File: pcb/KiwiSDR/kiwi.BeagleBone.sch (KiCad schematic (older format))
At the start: 18 parts, among them U1 Artix-7 A35, U301 EEPROM 32Kx8

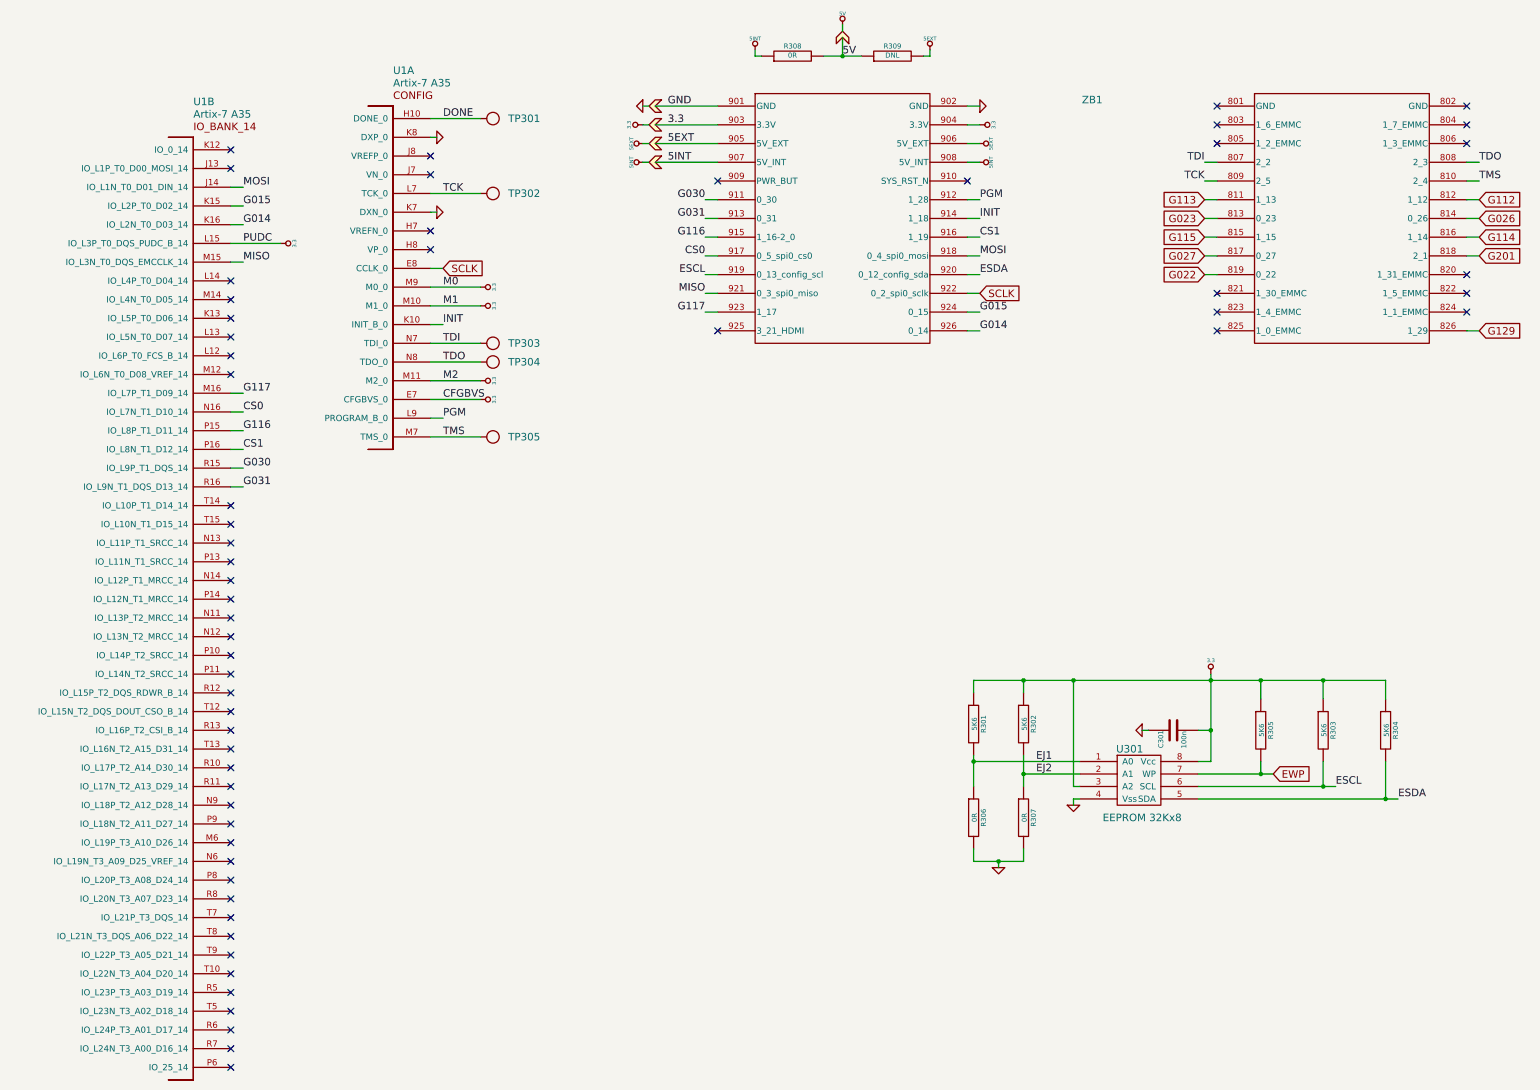
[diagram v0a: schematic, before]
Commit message: v0.5 PCB with 5V DC input
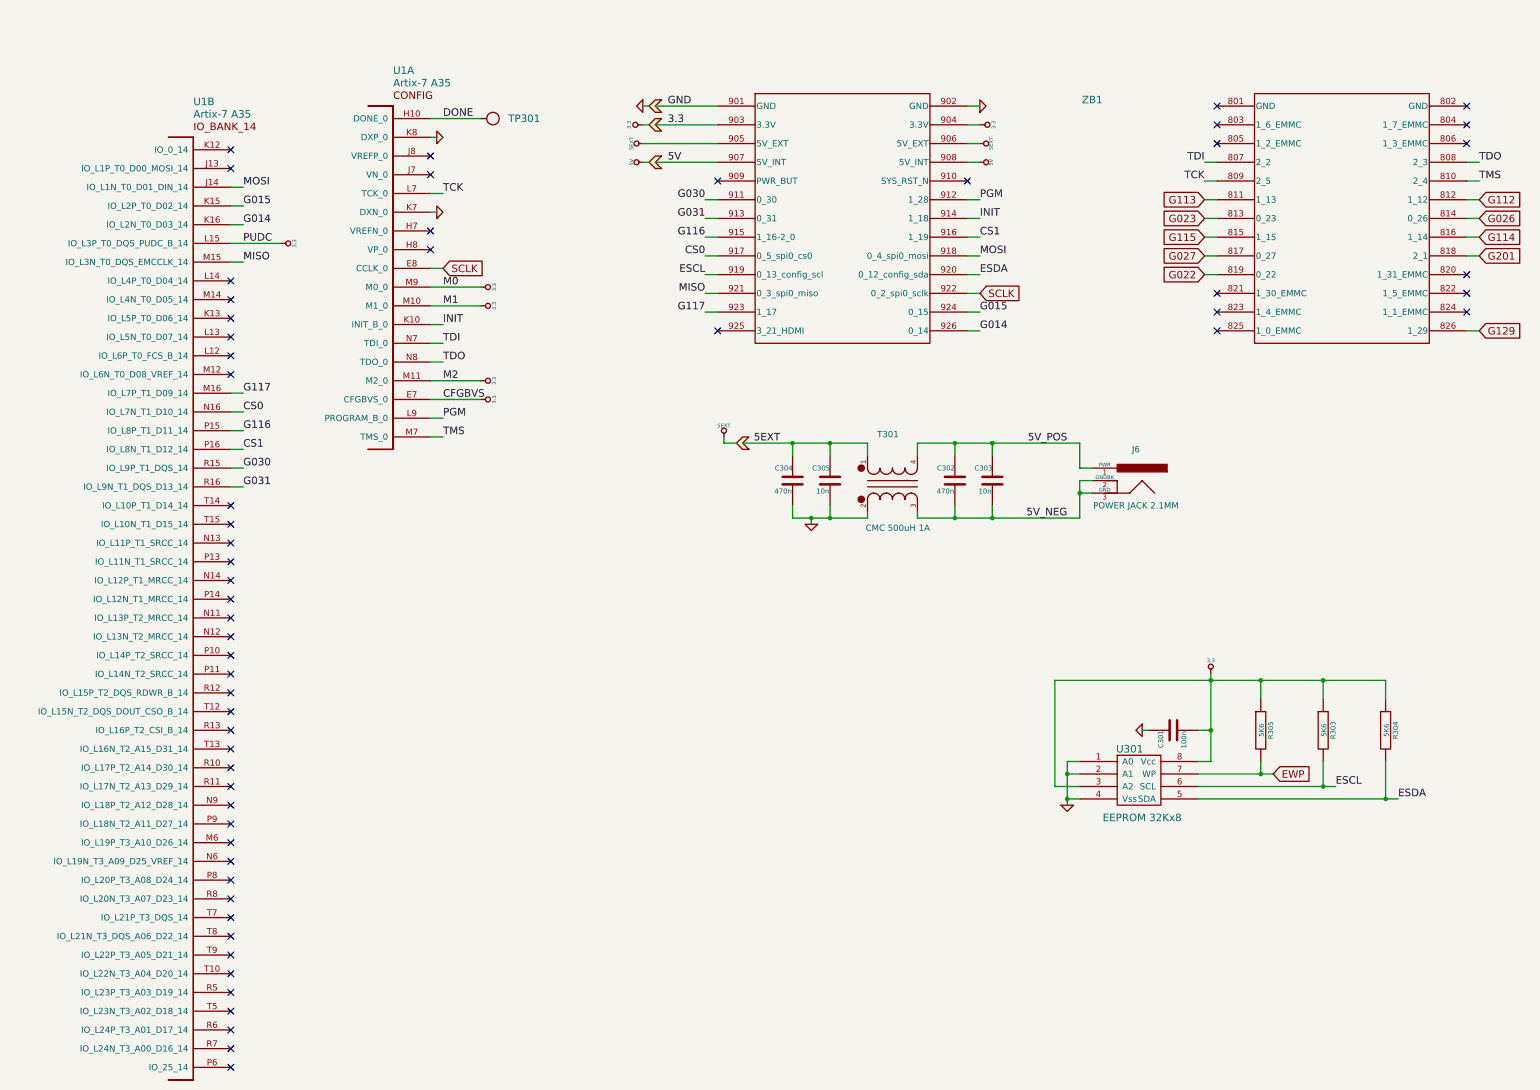
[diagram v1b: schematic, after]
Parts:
- removed R301, R302: 5K6, kiwi-SM0402, symbol R
- removed R306, R307: 0R, kiwi-SM0402, symbol R
- removed R308: 0R, kiwi-SM0805, symbol R
- removed R309: DNL, kiwi-SM0805, symbol R
- removed TP302, TP303: TEST_POINT, kiwi-TP_1250, symbol TEST_POINT
- removed TP304, TP305: TEST_POINT, kiwi-TP_VIA_1250, symbol TEST_POINT
- added C302, C304: 470n, kiwi-SM0402, symbol C
- added C303, C305: 10n, kiwi-SM0402, symbol C
- added J6: POWER JACK 2.1MM, kiwi-JACK_2_1MM_TH, symbol POWER_JACK
- added T301: CMC 500uH 1A, kiwi-CMC, symbol COMMON_MODE_CHOKE
- ZB1: value BEAGLEBONE_BLACK -> HEADER 13x2
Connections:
- net 5INT is gone; now on net 5V: ZB1.907 (5V_INT), ZB1.908 (5V_INT)
- net EJ1 is gone; now on net GND: U301.1 (A0)
- net EJ2 is gone; now on net GND: U301.2 (A1)
- net 5EXT: now also C304.1, C305.1, T301.1
- net GND: now also C304.2, C305.2, T301.2
- new net 5V_NEG: C302.2, C303.2, J6.2 (GNDBK), J6.3 (GND), T301.3
- new net 5V_POS: C302.1, C303.1, J6.1 (PWR), T301.4
